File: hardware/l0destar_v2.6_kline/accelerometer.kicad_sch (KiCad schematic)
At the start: 4 parts

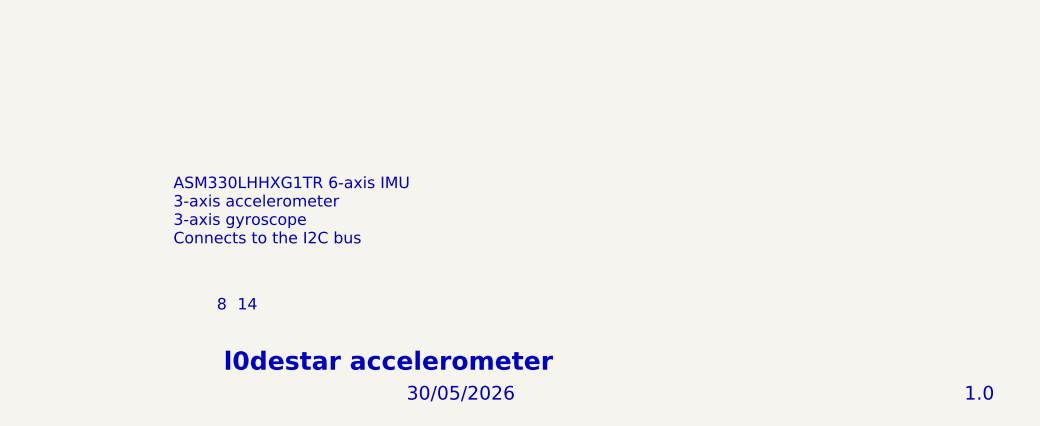
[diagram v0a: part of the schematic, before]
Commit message: fix sheet annotations
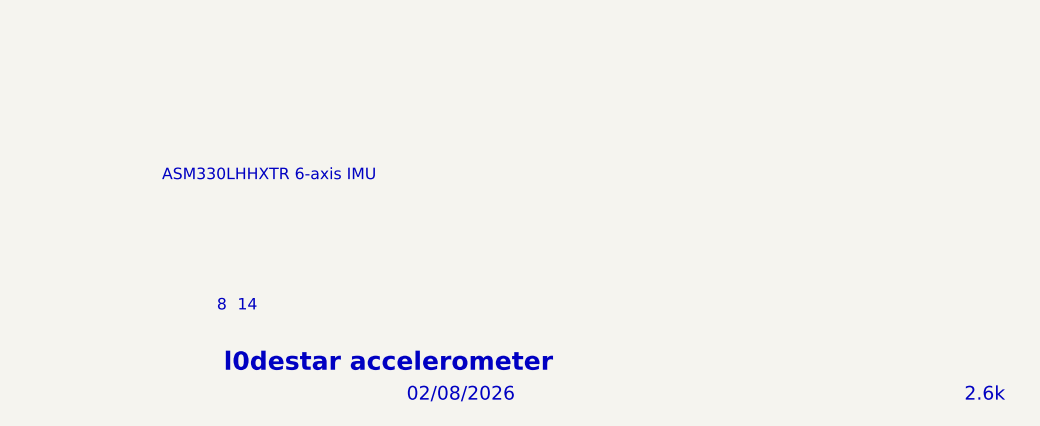
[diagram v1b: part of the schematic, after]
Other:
- note added: "02/08/2026"
- note added: "2.6k"
- note added: "ASM330LHHXTR 6-axis IMU"
- note removed: "1.0"
- note removed: "30/05/2026"
- note removed: "ASM330LHHXG1TR 6-axis IMU 3-axis accelerometer 3-axis gyroscope Connects to the I2C bus"
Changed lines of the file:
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@@
 	(generator_version "10.0")
 	(paper "A4")
-	(text "30/05/2026"
+	(text "02/08/2026"
 		(exclude_from_sim no)
 		(at 206.248 193.294 0)
@@
 		)
 	)
-	(text "ASM330LHHXG1TR 6-axis IMU\n3-axis accelerometer\n3-axis gyroscope\nConnects to the I2C bus"
+	(text "ASM330LHHXTR 6-axis IMU"
 		(exclude_from_sim no)
-		(at 180.34 172.974 0)
+		(at 179.07 168.91 0)
 		(effects
 			(font
@@
 		)
 	)
-	(text "1.0"
+	(text "2.6k"
 		(exclude_from_sim no)
 		(at 268.224 193.294 0)
